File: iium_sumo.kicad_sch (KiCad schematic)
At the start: 51 parts, among them J1 I2C_VL53_1, J10 Cytron MD, J11 Cytron Start Module, J12 Conn_01x05, J13 Conn_01x05, J14 Conn_01x05, J15 Conn_01x15_Pin, J16 Conn_01x02_Pin, J17 Conn_01x02_Pin, J2 I2C_VL53_2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

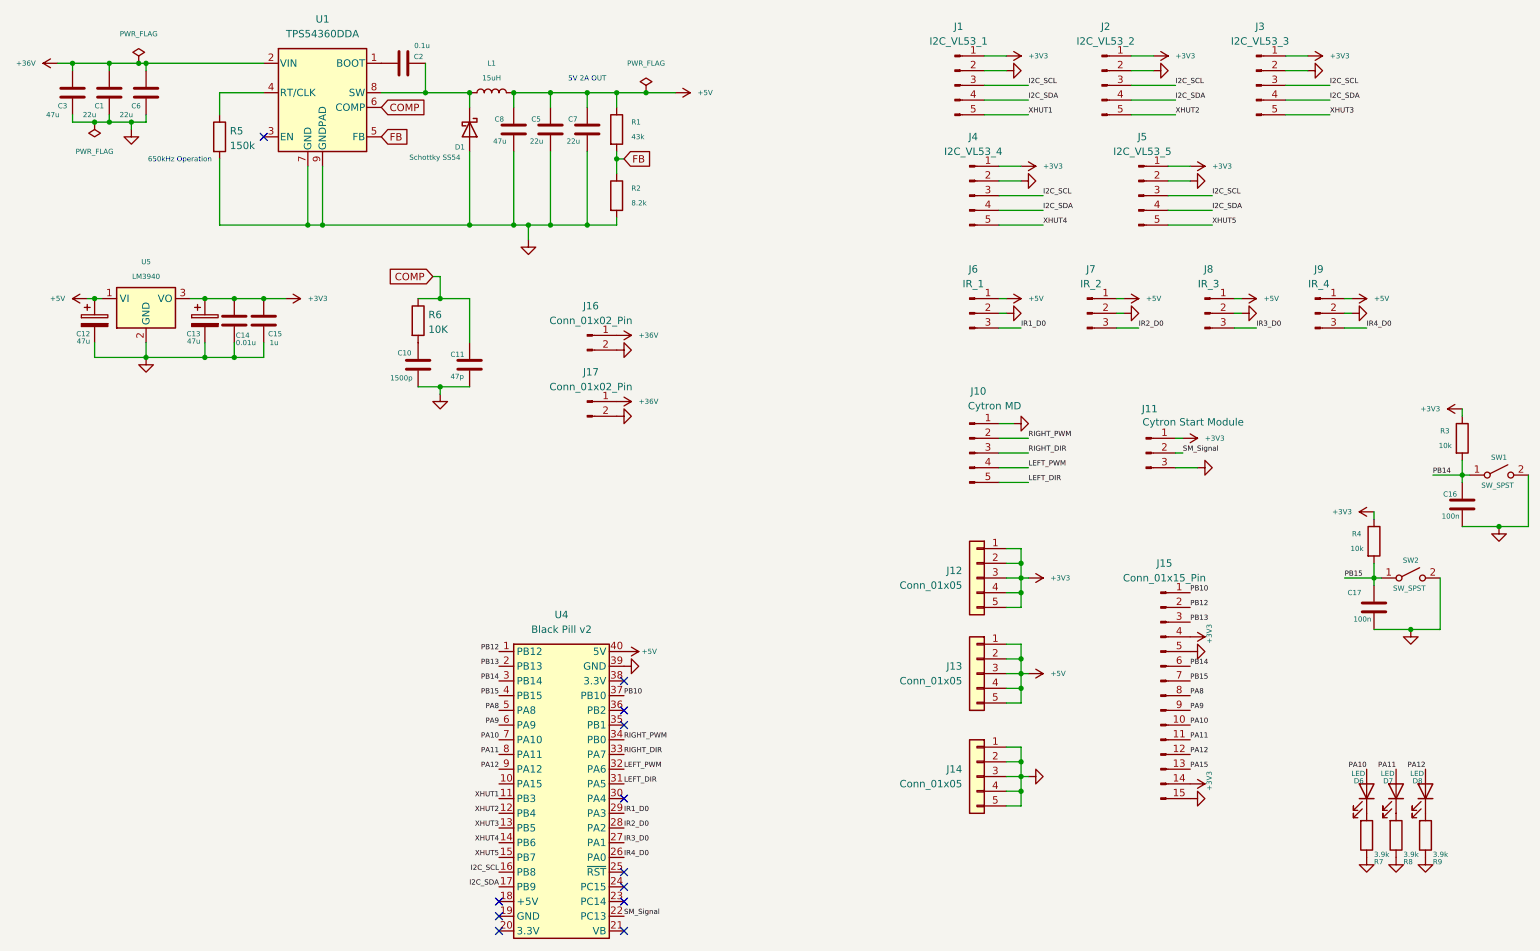
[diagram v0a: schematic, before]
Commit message: Add UART interface and update PCB design
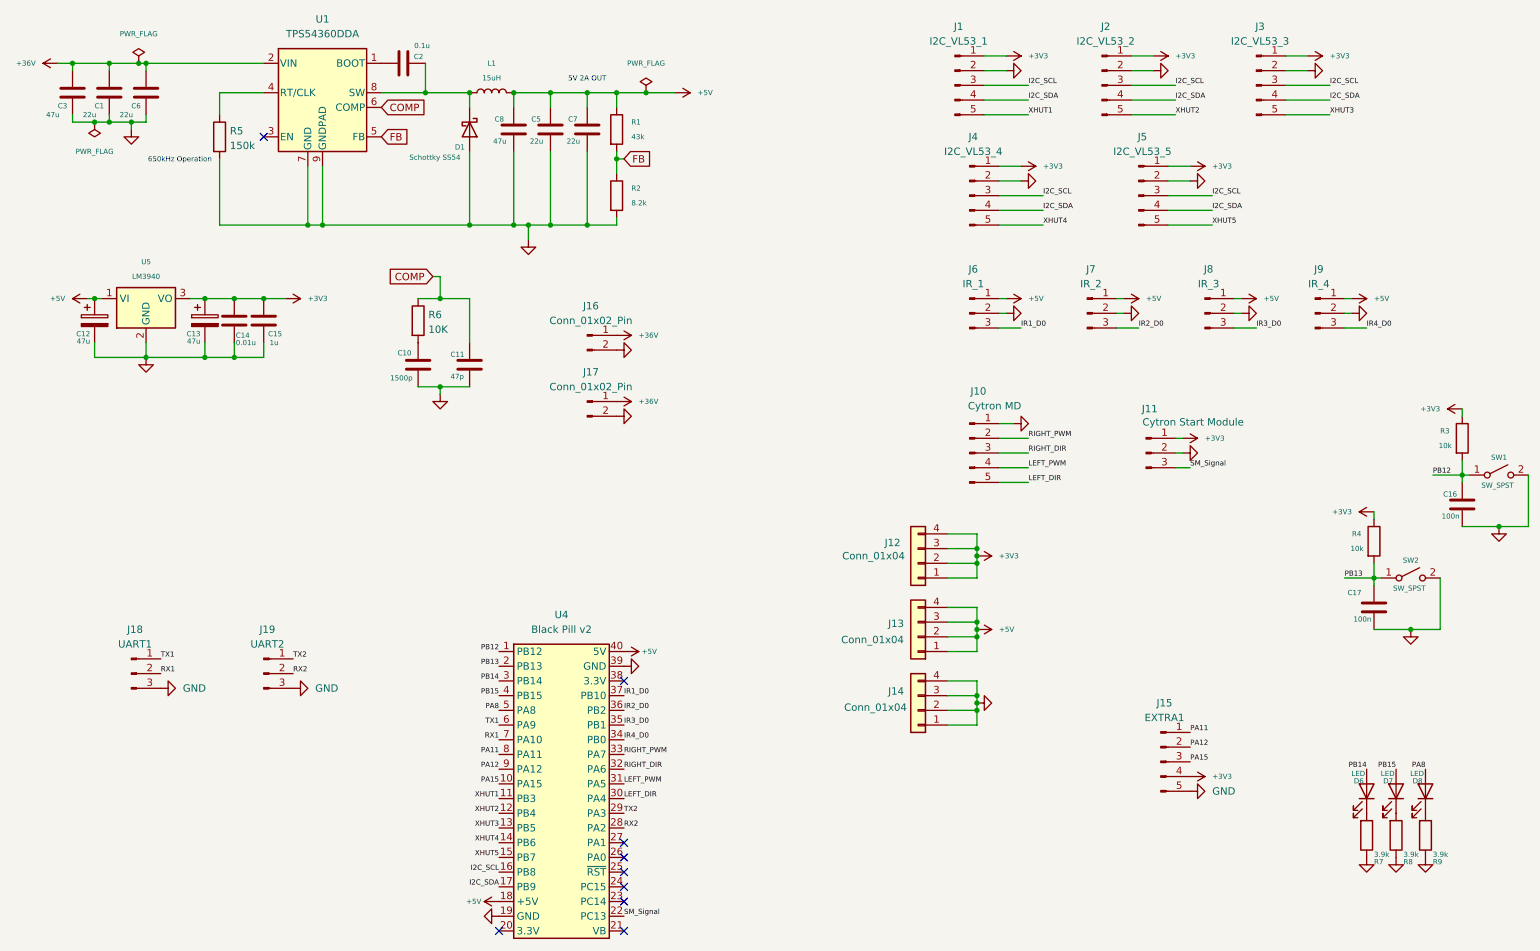
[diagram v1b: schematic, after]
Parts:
- removed J12, J13, J14: Conn_01x05, Connector_PinHeader_2.54mm:PinHeader_1x05_P2.54mm_Vertical, symbol Connector_Generic:Conn_01x05
- removed J15: Conn_01x15_Pin, Connector_Molex:Molex_KK-254_AE-6410-15A_1x15_P2.54mm_Vertical, symbol Connector:Conn_01x15_Pin
- added J12, J13, J14: Conn_01x04, Connector_PinHeader_1.00mm:PinHeader_1x04_P1.00mm_Vertical, symbol Connector_Generic:Conn_01x04
- added J15: EXTRA1, Connector_Molex:Molex_KK-254_AE-6410-05A_1x05_P2.54mm_Vertical, symbol Connector:Conn_01x05_Pin
- added J18: UART1, Connector_Molex:Molex_KK-254_AE-6410-03A_1x03_P2.54mm_Vertical, symbol Connector:Conn_01x03_Pin
- added J19: UART2, Connector_Molex:Molex_KK-254_AE-6410-03A_1x03_P2.54mm_Vertical, symbol Connector:Conn_01x03_Pin
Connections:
- net PB10 is gone; now on net IR1_D0: U4.37 (PB10)
- net +3V3: now also J12.1 (Pin_1), J12.2 (Pin_2), J12.3 (Pin_3), J12.4 (Pin_4), J15.4 (Pin_4)
- net +5V: now also U4.18 (+5V), J13.1 (Pin_1), J13.2 (Pin_2), J13.3 (Pin_3), J13.4 (Pin_4)
- net GND: now also J11.2 (Pin_2), U4.19 (GND), J14.1 (Pin_1), J14.2 (Pin_2), J14.3 (Pin_3), J14.4 (Pin_4), J15.5 (Pin_5), J18.3 (Pin_3), J19.3 (Pin_3); no longer J11.3 (Pin_3)
- net IR1_D0: no longer U4.29 (PA3)
- net IR2_D0: now also U4.36 (PB2); no longer U4.28 (PA2)
- net IR3_D0: now also U4.35 (PB1); no longer U4.27 (PA1)
- net IR4_D0: now also U4.34 (PB0); no longer U4.26 (PA0)
- net LEFT_DIR: now also U4.30 (PA4); no longer U4.31 (PA5)
- net LEFT_PWM: now also U4.31 (PA5); no longer U4.32 (PA6)
- net PA11: now also J15.1 (Pin_1); no longer D7.2 (A)
- net PA12: now also J15.2 (Pin_2); no longer D8.2 (A)
- net PA15: now also U4.10 (PA15), J15.3 (Pin_3)
- net PA8: now also D8.2 (A)
- net PB12: now also C16.1, R3.2, SW1.1 (A)
- net PB13: now also C17.1, R4.2, SW2.1 (A)
- net PB14: now also D6.2 (A); no longer C16.1, R3.2, SW1.1 (A)
- net PB15: now also D7.2 (A); no longer C17.1, R4.2, SW2.1 (A)
- net RIGHT_DIR: now also U4.32 (PA6); no longer U4.33 (PA7)
- net RIGHT_PWM: now also U4.33 (PA7); no longer U4.34 (PB0)
- net SM_Signal: now also J11.3 (Pin_3); no longer J11.2 (Pin_2)
- net PA10 renamed RX1
- net RX1: now also J18.2 (Pin_2); no longer D6.2 (A)
- net PA9 renamed TX1
- net TX1: now also J18.1 (Pin_1)
- new net RX2: J19.2 (Pin_2), U4.28 (PA2)
- new net TX2: J19.1 (Pin_1), U4.29 (PA3)
- no-connect marks 12 -> 9

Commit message: fixed errors
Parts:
- J12, J13, J14: footprint Connector_PinHeader_1.00mm:PinHeader_1x04_P1.00mm_Vertical -> Connector_PinHeader_2.54mm:PinHeader_1x04_P2.54mm_Vertical
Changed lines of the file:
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@@
 			)
 		)
-		(property "Footprint" "Connector_PinHeader_1.00mm:PinHeader_1x04_P1.00mm_Vertical"
+		(property "Footprint" "Connector_PinHeader_2.54mm:PinHeader_1x04_P2.54mm_Vertical"
 			(at 172.72 132.08 0)
 			(hide yes)
@@
 			)
 		)
-		(property "Footprint" "Connector_PinHeader_1.00mm:PinHeader_1x04_P1.00mm_Vertical"
+		(property "Footprint" "Connector_PinHeader_2.54mm:PinHeader_1x04_P2.54mm_Vertical"
 			(at 172.72 119.38 0)
 			(hide yes)
@@
 			)
 		)
-		(property "Footprint" "Connector_PinHeader_1.00mm:PinHeader_1x04_P1.00mm_Vertical"
+		(property "Footprint" "Connector_PinHeader_2.54mm:PinHeader_1x04_P2.54mm_Vertical"
 			(at 172.72 106.68 0)
 			(hide yes)
